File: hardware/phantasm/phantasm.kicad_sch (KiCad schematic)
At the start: 29 parts, among them J1 +5V IN ~1A, J2 LED sig DI/CI/SIG_GND, J3A SYNC in, J3B SYNC out, J4 debug, U1 74AHCT125

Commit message: pcb: complete PHANTASM fabrication safeguards
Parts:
- removed Q_REV: B5819W, Diode_SMD:D_SOD-123, symbol Device:D_Schottky
- added Q_REV: AO3401A, Package_TO_SOT_SMD:SOT-23, symbol Transistor_FET:Q_PMOS_GSD
- F1: value 0.5A -> 0.5A hold
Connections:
- net +5V_PROT: now also Q_REV.2 (S)
- net +5V_RAW: now also Q_REV.3 (D)
- net GND: now also Q_REV.1 (G)

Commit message: phantasm: finalize routed PCB and fabrication gates
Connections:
- net +5V_LOGIC: no longer U1.13
- net GND: no longer R_PD.2
- net MASTER_EN: now also U1.13
- net SYNC_PULLDOWN: now reaches U1.11
- net SYNC_PULLDOWN: now also R_PD.2
- no-connect marks 1 -> 0
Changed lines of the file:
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@@
 		(color 0 0 0 0)
 	)
-	(no_connect
-		(at 160.02 228.6)
+	(label "SYNC_PULLDOWN"
+		(at 160.02 228.6 0)
+		(effects (font (size 1.27 1.27)) (justify left bottom))
 	)
 	(wire
@@
 		(effects (font (size 1.27 1.27)) (justify left bottom))
 	)
+	(label "MASTER_EN"
+		(at 152.4 237.49 0)
+		(effects (font (size 1.27 1.27)) (justify left bottom))
+	)
 	(label "DATA"
 		(at 273.05 162.56 0)
@@
 	(label "SYNC_BUS"
 		(at 292.1 198.12 0)
+		(effects (font (size 1.27 1.27)) (justify left bottom))
+	)
+	(label "SYNC_PULLDOWN"
+		(at 292.1 212.09 0)
 		(effects (font (size 1.27 1.27)) (justify left bottom))
 	)
@@
 			(effects (font (size 1.27 1.27)))
 		)
-		(property "Footprint" ""
+		(property "Footprint" "phantasm:Teensy4.0"
 			(at 33.02 66.04 0)
 			(effects (font (size 1.27 1.27)) (hide yes))
@@
 	(symbol
 		(lib_id "phantasm:+5V_LOGIC")
-		(at 152.4 237.49 0)
-		(unit 1)
-		(exclude_from_sim no)
-		(in_bom yes)
-		(on_board yes)
-		(dnp no)
-		(property "Reference" "#PWR"
-			(at 152.4 232.41 0)
-			(effects (font (size 1.27 1.27)))
-		)
-		(property "Value" "+5V_LOGIC"
-			(at 152.4 242.57 0)
-			(effects (font (size 1.27 1.27)))
-		)
-		(property "Footprint" ""
-			(at 152.4 245.11 0)
-			(effects (font (size 1.27 1.27)) (hide yes))
-		)
-		(property "Datasheet" ""
-			(at 152.4 237.49 0)
-			(effects (font (size 1.27 1.27)) (hide yes))
-		)
-		(pin "1")
-		(instances
-			(project "phantasm"
-				(path "/928f299b-a262-40fe-9d10-61bd500c5b4b"
-					(reference "#PWR") (unit 1)
-				)
-			)
-		)
-	)
-	(symbol
-		(lib_id "phantasm:+5V_LOGIC")
 		(at 215.9 121.92 0)
 		(unit 1)
@@
 				)
 			)
-		)
-	)
-	(symbol
-		(lib_id "power:GND")
-		(at 292.1 212.09 0)
-		(unit 1)
-		(exclude_from_sim no)
-		(in_bom yes)
-		(on_board yes)
-		(dnp no)
-		(property "Reference" "#PWR"
-			(at 292.1 207.01 0)
-			(effects (font (size 1.27 1.27)))
-		)
-		(property "Value" "GND"
-			(at 292.1 217.17 0)
-			(effects (font (size 1.27 1.27)))
-		)
-		(property "Footprint" ""
-			(at 292.1 219.71 0)
-			(effects (font (size 1.27 1.27)) (hide yes))
-		)
-		(property "Datasheet" ""
-			(at 292.1 212.09 0)
-			(effects (font (size 1.27 1.27)) (hide yes))
-		)
-		(pin "1")
-		(instances
-			(project "phantasm"
-				(path "/928f299b-a262-40fe-9d10-61bd500c5b4b"
-					(reference "#PWR") (unit 1)
-				)
-			)

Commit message: PCB rev 1.1
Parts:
- removed R_ID0: 10k DNP, Resistor_SMD:R_0603_1608Metric, symbol Device:R
- D_BUS: value TVS -> CDSOD323-T05L; now fitted
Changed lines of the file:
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@@
-	)
-	(wire
-		(pts (xy 101.6 257.81) (xy 101.6 255.27))
-		(stroke (width 0) (type default))
-	)
-	(wire
-		(pts (xy 101.6 265.43) (xy 101.6 269.24))
-		(stroke (width 0) (type default))
 	)
 	(wire
@@
 	(label "MASTER_EN"
 		(at 76.2 269.24 0)
-		(effects (font (size 1.27 1.27)) (justify left bottom))
-	)
-	(label "ID0"
-		(at 101.6 269.24 0)
 		(effects (font (size 1.27 1.27)) (justify left bottom))
 	)
@@
 		(in_bom yes)
 		(on_board yes)
-		(dnp yes)
+		(dnp no)
 		(property "Reference" "D_BUS"
 			(at 292.1 226.06 0)
 			(effects (font (size 1.27 1.27)))
 		)
-		(property "Value" "TVS"
+		(property "Value" "CDSOD323-T05L"
 			(at 292.1 236.22 0)
 			(effects (font (size 1.27 1.27)))
@@
 			(effects (font (size 1.27 1.27)) (hide yes))
 		)
-		(property "Datasheet" ""
+		(property "Datasheet" "https://www.bourns.com/docs/Product-Datasheets/CDSOD323-TxxLC.pdf"
 			(at 292.1 231.14 0)
 			(effects (font (size 1.27 1.27)) (hide yes))
@@
 			(effects (font (size 1.27 1.27)) (hide yes))
 		)
-		(pin "1")
-		(instances
-			(project "phantasm"
-				(path "/928f299b-a262-40fe-9d10-61bd500c5b4b"
-					(reference "#PWR") (unit 1)
-				)
-			)
-		)
-	)
-	(symbol
-		(lib_id "Device:R")
-		(at 101.6 261.62 0)
-		(unit 1)
-		(exclude_from_sim no)
-		(in_bom yes)
-		(on_board yes)
-		(dnp yes)
-		(property "Reference" "R_ID0"
-			(at 101.6 256.54 0)
-			(effects (font (size 1.27 1.27)))
-		)
-		(property "Value" "10k DNP"
-			(at 101.6 266.7 0)
-			(effects (font (size 1.27 1.27)))
-		)
-		(property "Footprint" "Resistor_SMD:R_0603_1608Metric"
-			(at 101.6 269.24 0)
-			(effects (font (size 1.27 1.27)) (hide yes))
-		)
-		(property "Datasheet" ""
-			(at 101.6 261.62 0)
-			(effects (font (size 1.27 1.27)) (hide yes))
-		)
-		(pin "1")
-		(pin "2")
-		(instances
-			(project "phantasm"
-				(path "/928f299b-a262-40fe-9d10-61bd500c5b4b"
-					(reference "R_ID0") (unit 1)
-				)
-			)
-		)
-	)
-	(symbol
-		(lib_id "power:+3V3")
-		(at 101.6 255.27 0)
-		(unit 1)
-		(exclude_from_sim no)
-		(in_bom yes)
-		(on_board yes)
-		(dnp no)
-		(property "Reference" "#PWR"
-			(at 101.6 250.19 0)
-			(effects (font (size 1.27 1.27)))
-		)
-		(property "Value" "+3V3"
-			(at 101.6 260.35 0)
-			(effects (font (size 1.27 1.27)))
-		)
-		(property "Footprint" ""
-			(at 101.6 262.89 0)
-			(effects (font (size 1.27 1.27)) (hide yes))
-		)
-		(property "Datasheet" ""
-			(at 101.6 255.27 0)
-			(effects (font (size 1.27 1.27)) (hide yes))
-		)

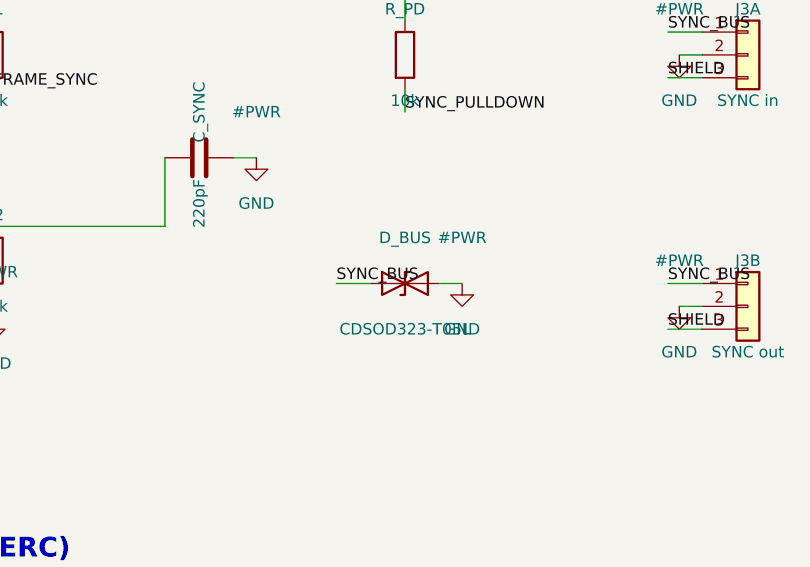
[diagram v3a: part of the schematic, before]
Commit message: phantasm: correct TVS polarity metadata and refill pours
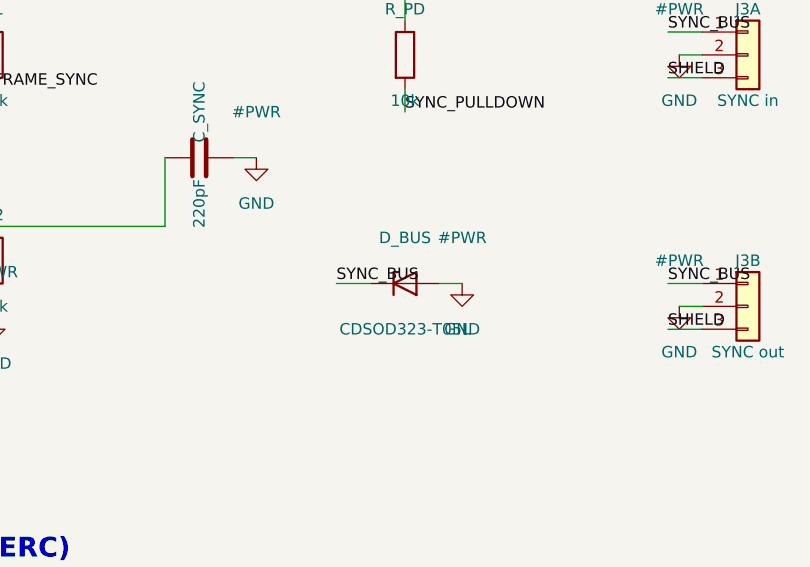
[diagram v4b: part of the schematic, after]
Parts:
- D_BUS: symbol Device:D_TVS -> Device:D_Zener
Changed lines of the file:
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@@
 	)
 	(symbol
-		(lib_id "Device:D_TVS")
+		(lib_id "Device:D_Zener")
 		(at 292.1 231.14 0)
 		(unit 1)
